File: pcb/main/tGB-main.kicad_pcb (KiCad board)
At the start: 2 copper layers, 51 x 61 mm, 70 parts, among them J1 GB-CardEdge, J2 PROG_PORT, Q1 DMG3415U, Q2 HN4A56JU, Q3 2N7002K, U1 TC74LCXR163245FT, U2 TC74LCXR163245FT, U3 ICE40UP5K-SG48ITR, U4 TPS79901DDCR, U5 TPS79901DDCR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

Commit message: common symbols and footprints
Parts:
- J2: footprint PinHeader:PinHeader-10P-Sidemount -> Pin_Sidemount:PinHeader_1x10_P2.54_Sidemount
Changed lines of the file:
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@@
       (net 54 "/DV-~{CS}") (pinfunction "1") (pintype "passive"))
   )
-  (footprint "PinHeader:PinHeader-10P-Sidemount" (layer "F.Cu")
+  (footprint "Pin_Sidemount:PinHeader_1x10_P2.54_Sidemount" (layer "F.Cu")
     (at 38.056 50.421)
     (property "Sheetfile" "tGB-main.kicad_sch")
     (property "Sheetname" "")
     (attr through_hole)
-    (fp_text reference "J2" (at 0 3.81) (layer "F.SilkS") hide
+    (fp_text reference "J2" (at 0 -4.064) (layer "F.SilkS") hide
       (effects (font (size 0.6 0.6) (thickness 0.12)))
     )
-    (fp_text value "PROG_PORT" (at 11.424 -2.471) (layer "F.Fab")
+    (fp_text value "PROG_PORT" (at 11.444 -2.521) (layer "F.Fab")
       (effects (font (size 0.6 0.6) (thickness 0.12)))
     )
@@
     (pad "1" smd rect (at 0 0) (size 1.7 3.25) (layers "F.Cu" "F.Mask")
       (net 1 "+5V") (pinfunction "Pin_1") (pintype "passive"))
+    (pad "2" smd rect (at 2.54 0) (size 1.7 3.25) (layers "F.Cu" "F.Mask")
+      (net 3 "+3V3") (pinfunction "Pin_2") (pintype "passive"))
     (pad "2" thru_hole rect (at 2.54 -0.775) (size 1.7 1.7) (drill 1) (layers *.Cu *.Mask)
       (net 3 "+3V3") (pinfunction "Pin_2") (pintype "passive"))
-    (pad "2" smd rect (at 2.54 0) (size 1.7 3.25) (layers "F.Cu" "F.Mask")
-      (net 3 "+3V3") (pinfunction "Pin_2") (pintype "passive"))
+    (pad "3" smd rect (at 5.08 0) (size 1.7 3.25) (layers "F.Cu" "F.Mask")
+      (net 2 "GND") (pinfunction "Pin_3") (pintype "passive"))
     (pad "3" thru_hole rect (at 5.08 -0.775) (size 1.7 1.7) (drill 1) (layers *.Cu *.Mask)
-      (net 2 "GND") (pinfunction "Pin_3") (pintype "passive"))
-    (pad "3" smd rect (at 5.08 0) (size 1.7 3.25) (layers "F.Cu" "F.Mask")
       (net 2 "GND") (pinfunction "Pin_3") (pintype "passive"))
     (pad "4" smd rect (at 7.62 0) (size 1.7 3.25) (layers "F.Cu" "F.Mask")
@@
     (pad "5" smd rect (at 10.16 0) (size 1.7 3.25) (layers "F.Cu" "F.Mask")
       (net 49 "/SPI-MOSI") (pinfunction "Pin_5") (pintype "passive"))
+    (pad "6" smd rect (at 12.7 0) (size 1.7 3.25) (layers "F.Cu" "F.Mask")
+      (net 50 "/SPI-SS") (pinfunction "Pin_6") (pintype "passive"))
     (pad "6" thru_hole rect (at 12.7 -0.775) (size 1.7 1.7) (drill 1) (layers *.Cu *.Mask)
       (net 50 "/SPI-SS") (pinfunction "Pin_6") (pintype "passive"))
-    (pad "6" smd rect (at 12.7 0) (size 1.7 3.25) (layers "F.Cu" "F.Mask")
-      (net 50 "/SPI-SS") (pinfunction "Pin_6") (pintype "passive"))
+    (pad "7" thru_hole rect (at 15.24 -0.775) (size 1.7 1.7) (drill 1) (layers *.Cu *.Mask)
+      (net 51 "/SPI-MISO") (pinfunction "Pin_7") (pintype "passive"))
     (pad "7" smd rect (at 15.24 0) (size 1.7 3.25) (layers "F.Cu" "F.Mask")
       (net 51 "/SPI-MISO") (pinfunction "Pin_7") (pintype "passive"))
-    (pad "7" thru_hole rect (at 15.24 -0.775) (size 1.7 1.7) (drill 1) (layers *.Cu *.Mask)
-      (net 51 "/SPI-MISO") (pinfunction "Pin_7") (pintype "passive"))
     (pad "8" smd rect (at 17.78 0) (size 1.7 3.25) (layers "F.Cu" "F.Mask")

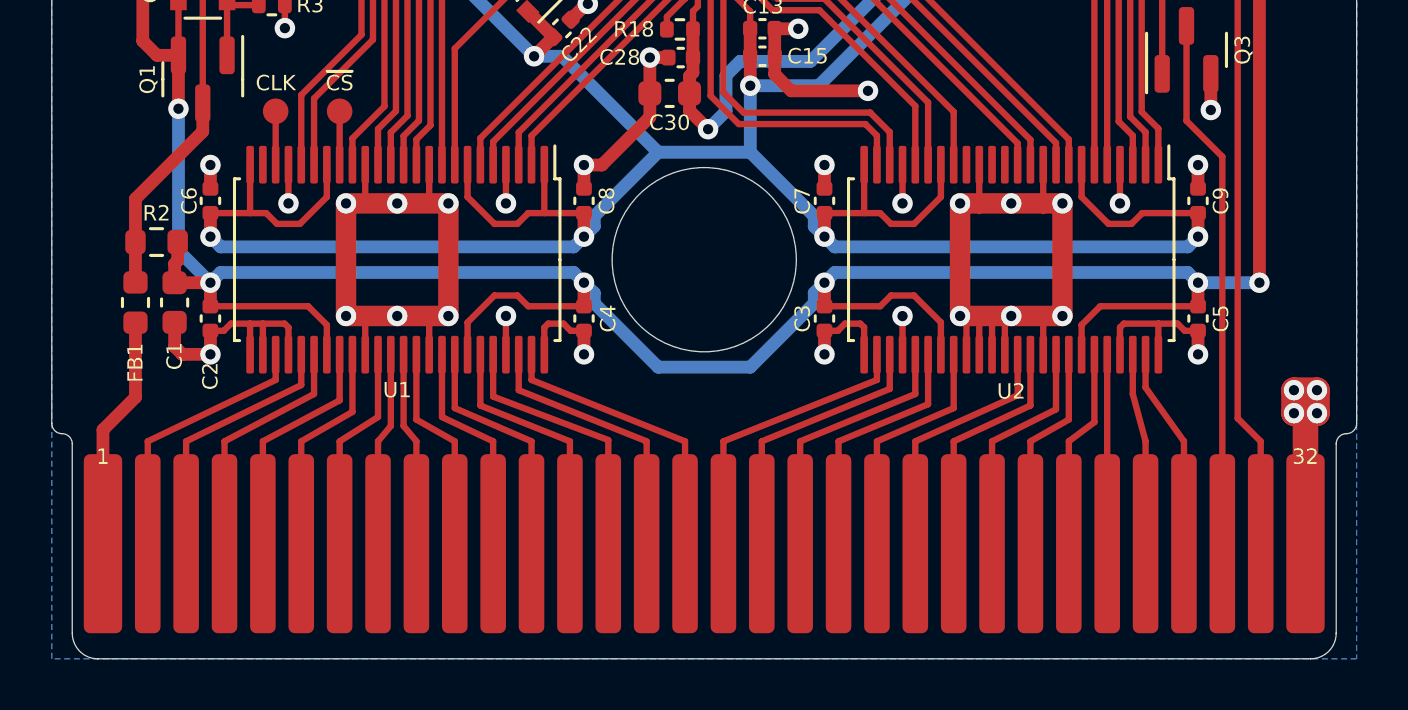
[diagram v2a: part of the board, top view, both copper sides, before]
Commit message: migration from KiCad 6 to 7
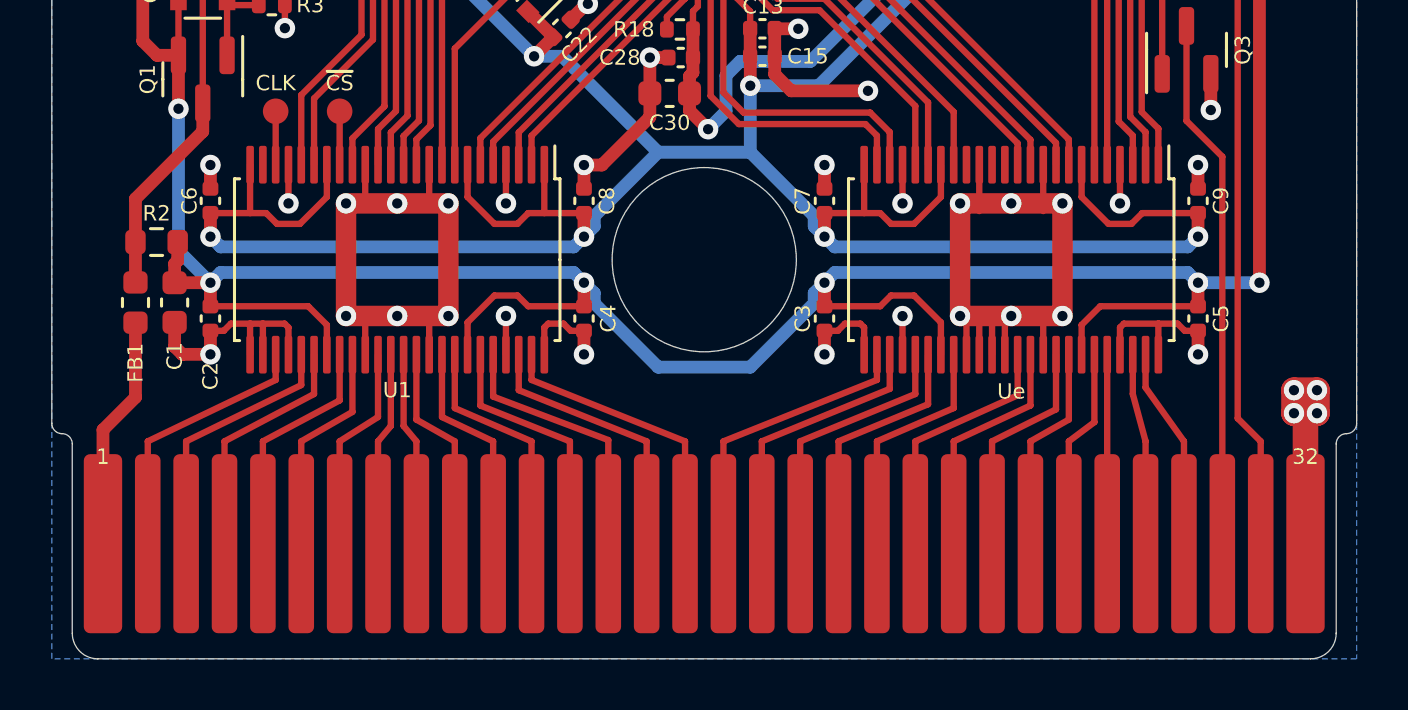
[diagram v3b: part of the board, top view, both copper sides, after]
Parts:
- renumbered U2 to Ue
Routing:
- net /CB-A7: track 9.76 -> 6.76 mm
- net /VCC: track 9.16 -> 6.16 mm
- net /CB-~{WR}: track 10.2 -> 7.20 mm
- net /CB-~{RD}: track 9.50 -> 6.50 mm
- net /CB-~{CS}: track 9.19 -> 6.19 mm
- net /CB-VIN: track 36.1 -> 33.1 mm
- net /CB-D7: track 7.87 -> 4.87 mm
- net /CB-D6: track 7.45 -> 4.45 mm
- net /CB-D5: track 7.39 -> 4.39 mm
- net /CB-D4: track 7.89 -> 4.89 mm
- net /CB-D3: track 8.26 -> 5.26 mm
- net /CB-D0: track 9.97 -> 6.97 mm
- net /CB-CLK: track 10.5 -> 7.53 mm
- net /CB-A9: track 10.8 -> 7.77 mm
- net /CB-A8: track 10.5 -> 7.50 mm
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
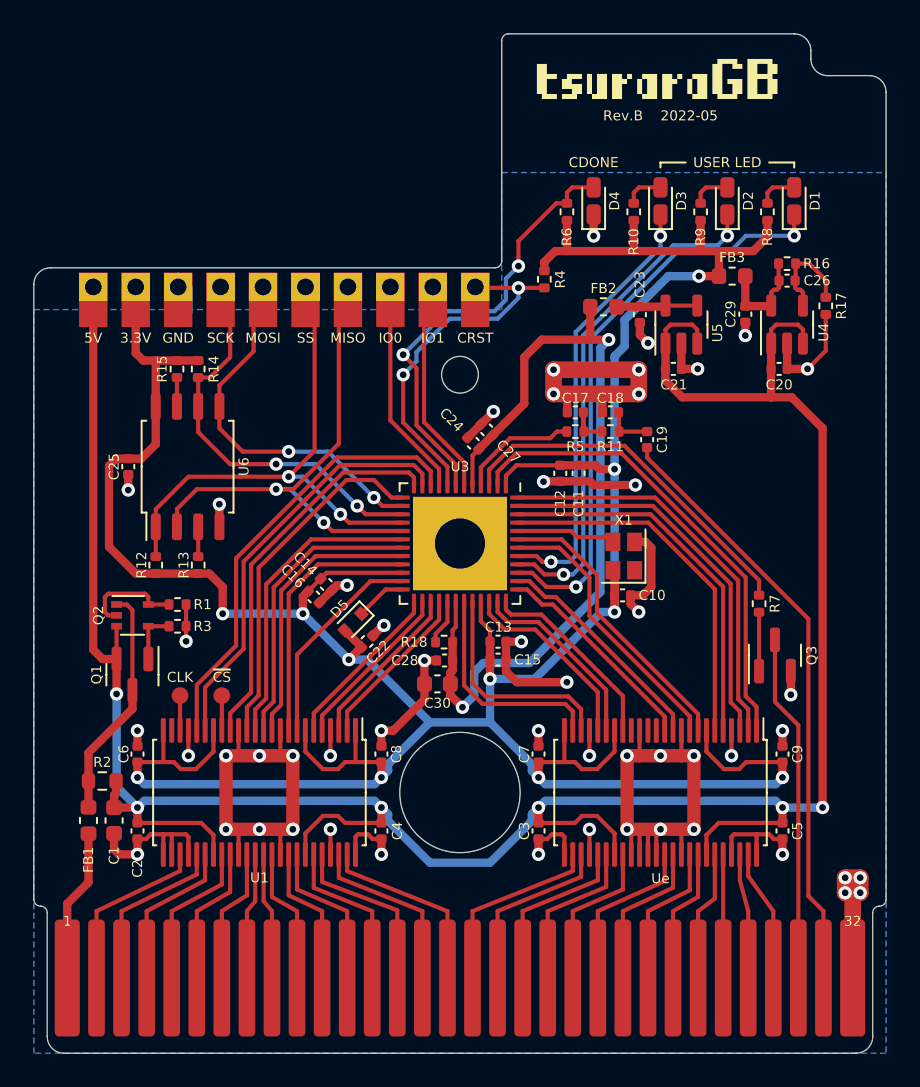
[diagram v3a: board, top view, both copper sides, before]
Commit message: migrate KiCad 7 -> 10
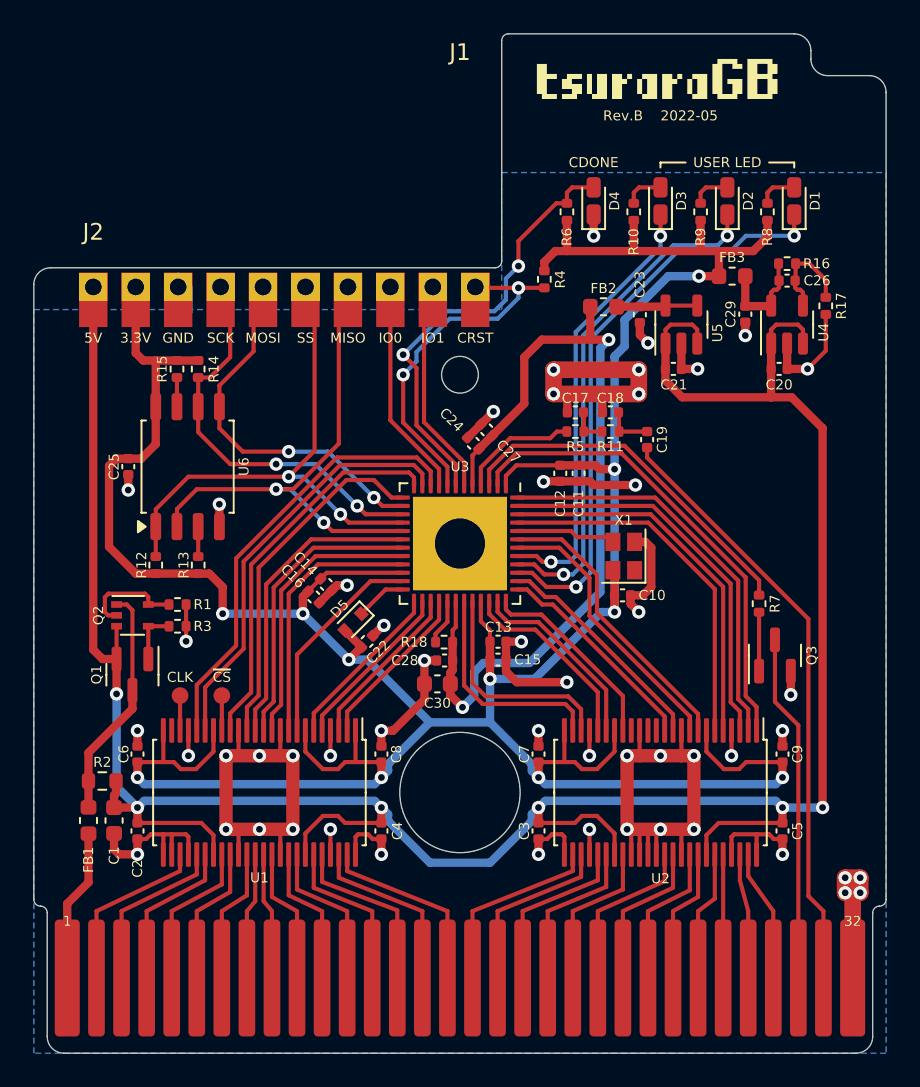
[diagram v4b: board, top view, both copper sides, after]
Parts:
- C19: value 1uF -> 1μF
- D1, D2, D3, D4: footprint LED_SMD:LED_0603_1608Metric_Castellated -> ProjectSpecific:LED_0603_1608Metric_Castellated
- J1: footprint GB-CardEdge:GB-CardEdge -> ProjectSpecific:GB-CardEdge
- J2: footprint Pin_Sidemount:PinHeader_1x10_P2.54_Sidemount -> ProjectSpecific:PinHeader_1x10_P2.54_Sidemount
- U6: footprint Package_SO:SOIC-8_5.275x5.275mm_P1.27mm -> Package_SO:SOIC-8_5.3x5.3mm_P1.27mm
- renumbered Ue to U2
